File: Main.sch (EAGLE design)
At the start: 47 parts, among them IC1 LM75A, IC2 ADUM1400, IC3 74LS14N, Q1 IRF9530, U1 L298, U2 LM 1084 IT5,0, U3 LM 1084 IT3,3, U4 L298, X1 Motors, X2 PIRs, X3 Battery, X4 Ultra Sonics

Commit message: playing with routes
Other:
- moved on the sheet: F2, IC2, SV1

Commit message: cleanup and started to add servo control
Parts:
- added OK3: PC847, optocoupler:PC847
- added R10, R11, R12, R13: 120, resistor:R-EU_R0805
- added X5: ITG-3200, con-wago:233-504
- added X6: PIRs, con-wago:233-506
- X2: value PIRs -> (none); device con-wago:233-512 -> con-ria-59:AKL59-04
- X4: value Ultra Sonics -> Ultra Sonics (5V); device con-wago:233-508 -> con-wago:233-506
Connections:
- new net N$13: OK3A.A, R10.2
- new net N$21: OK3B.A, R11.2
- new net N$23: OK3C.A, R12.2
- new net N$25: OK3D.A, R13.2
- net +12V: now also X2-1.1
- net +3.3V: now also X2-3.1, X5.B-1
- net +5V: now also OK3A.COL, OK3B.COL, X2-2.1, X6.B-5; no longer X2.B-12, X2.B-3, X2.B-6, X2.B-9, X4.B-7
- net GND: now also OK3A.C, OK3B.C, OK3C.C, OK3D.C, X2-4.1, X5.B-2, X6.B-6; no longer X2.B-1, X2.B-10, X2.B-4, X2.B-7, X4.B-8
- net PIR1: now also X6.B-1; no longer X2.B-2
- net PIR2: now also X6.B-2; no longer X2.B-5
- net PIR3: now also X6.B-3; no longer X2.B-8
- net PIR4: now also X6.B-4; no longer X2.B-11
- net SCL1: now also X5.B-4
- net SDA1: now also X5.B-3

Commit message: optimizing board
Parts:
- X6: value PIRs -> PIRs (5V); device con-wago:233-506 -> con-wago:233-504
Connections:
- net +5V: no longer X6.B-5
- net GND: no longer X6.B-6
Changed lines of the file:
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@@
 <part name="OK3" library="optocoupler" deviceset="PC847" device=""/>
 <part name="X5" library="con-wago" deviceset="233-504" device="" value="ITG-3200"/>
-<part name="X6" library="con-wago" deviceset="233-506" device="" value="PIRs"/>
-<part name="GND17" library="supply1" deviceset="GND" device=""/>
+<part name="X6" library="con-wago" deviceset="233-504" device="" value="PIRs (5V)"/>
 <part name="R10" library="resistor" deviceset="R-EU_" device="R0805" value="120"/>
 <part name="R11" library="resistor" deviceset="R-EU_" device="R0805" value="120"/>
@@
 <instance part="OK3" gate="D" x="-386.08" y="-302.26"/>
 <instance part="X5" gate="G$1" x="-441.96" y="-533.4"/>
-<instance part="X6" gate="G$1" x="-429.26" y="-15.24"/>
-<instance part="GND17" gate="1" x="-454.66" y="-27.94"/>
+<instance part="X6" gate="G$1" x="-429.26" y="-12.7"/>
 <instance part="R10" gate="G$1" x="-406.4" y="-246.38"/>
 <instance part="R11" gate="G$1" x="-406.4" y="-264.16"/>
@@
 <junction x="-457.2" y="513.08"/>
 <label x="-474.98" y="513.08" size="1.778" layer="95"/>
-</segment>
-<segment>
-<pinref part="X6" gate="G$1" pin="B-5"/>
-<wire x1="-436.88" y1="-20.32" x2="-454.66" y2="-20.32" width="0.1524" layer="91"/>
-<label x="-454.66" y="-20.32" size="1.778" layer="95"/>
 </segment>
 <segment>
@@
 </segment>
 <segment>
-<pinref part="X6" gate="G$1" pin="B-6"/>
-<wire x1="-436.88" y1="-22.86" x2="-454.66" y2="-22.86" width="0.1524" layer="91"/>
-<label x="-454.66" y="-22.86" size="1.778" layer="95"/>
-<pinref part="GND17" gate="1" pin="GND"/>
-<wire x1="-454.66" y1="-22.86" x2="-454.66" y2="-25.4" width="0.1524" layer="91"/>
-</segment>
-<segment>

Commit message: optimizing board
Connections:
- net PIR1: now also SV1.32; no longer SV1.40
- net PIR4: now also SV1.40; no longer SV1.32
- net SCL1: now also X5.B-3; no longer X5.B-4
- net SDA1: now also X5.B-4; no longer X5.B-3
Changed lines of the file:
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@@
 <net name="PIR1" class="0">
-<segment>
-<pinref part="SV1" gate="G$1" pin="40"/>
-<wire x1="-345.44" y1="528.32" x2="-320.04" y2="528.32" width="0.1524" layer="91"/>
-<label x="-320.04" y="528.32" size="1.778" layer="95"/>
-</segment>
 <segment>
 <pinref part="X6" gate="G$1" pin="B-1"/>
 <wire x1="-436.88" y1="-10.16" x2="-454.66" y2="-10.16" width="0.1524" layer="91"/>
 <label x="-454.66" y="-10.16" size="1.778" layer="95"/>
+</segment>
+<segment>
+<pinref part="SV1" gate="G$1" pin="32"/>
+<wire x1="-345.44" y1="518.16" x2="-320.04" y2="518.16" width="0.1524" layer="91"/>
+<label x="-320.04" y="518.16" size="1.778" layer="95"/>
 </segment>
 </net>
@@
 <net name="PIR4" class="0">
 <segment>
-<pinref part="SV1" gate="G$1" pin="32"/>
-<wire x1="-345.44" y1="518.16" x2="-320.04" y2="518.16" width="0.1524" layer="91"/>
-<label x="-320.04" y="518.16" size="1.778" layer="95"/>
-</segment>
-<segment>
 <pinref part="X6" gate="G$1" pin="B-4"/>
 <wire x1="-436.88" y1="-17.78" x2="-454.66" y2="-17.78" width="0.1524" layer="91"/>
 <label x="-454.66" y="-17.78" size="1.778" layer="95"/>
+</segment>
+<segment>
+<pinref part="SV1" gate="G$1" pin="40"/>
+<wire x1="-345.44" y1="528.32" x2="-320.04" y2="528.32" width="0.1524" layer="91"/>
+<label x="-320.04" y="528.32" size="1.778" layer="95"/>
 </segment>
 </net>
@@
 </segment>
 <segment>
-<pinref part="X5" gate="G$1" pin="B-3"/>
-<wire x1="-449.58" y1="-535.94" x2="-487.68" y2="-535.94" width="0.1524" layer="91"/>
-<label x="-487.68" y="-535.94" size="1.778" layer="95"/>
+<pinref part="X5" gate="G$1" pin="B-4"/>
+<wire x1="-449.58" y1="-538.48" x2="-487.68" y2="-538.48" width="0.1524" layer="91"/>
+<label x="-487.68" y="-538.48" size="1.778" layer="95"/>
 </segment>
 </net>
@@
 </segment>
 <segment>
-<pinref part="X5" gate="G$1" pin="B-4"/>
-<wire x1="-449.58" y1="-538.48" x2="-487.68" y2="-538.48" width="0.1524" layer="91"/>
-<label x="-487.68" y="-538.48" size="1.778" layer="95"/>
+<pinref part="X5" gate="G$1" pin="B-3"/>
+<wire x1="-449.58" y1="-535.94" x2="-487.68" y2="-535.94" width="0.1524" layer="91"/>
+<label x="-487.68" y="-535.94" size="1.778" layer="95"/>
 </segment>
 </net>

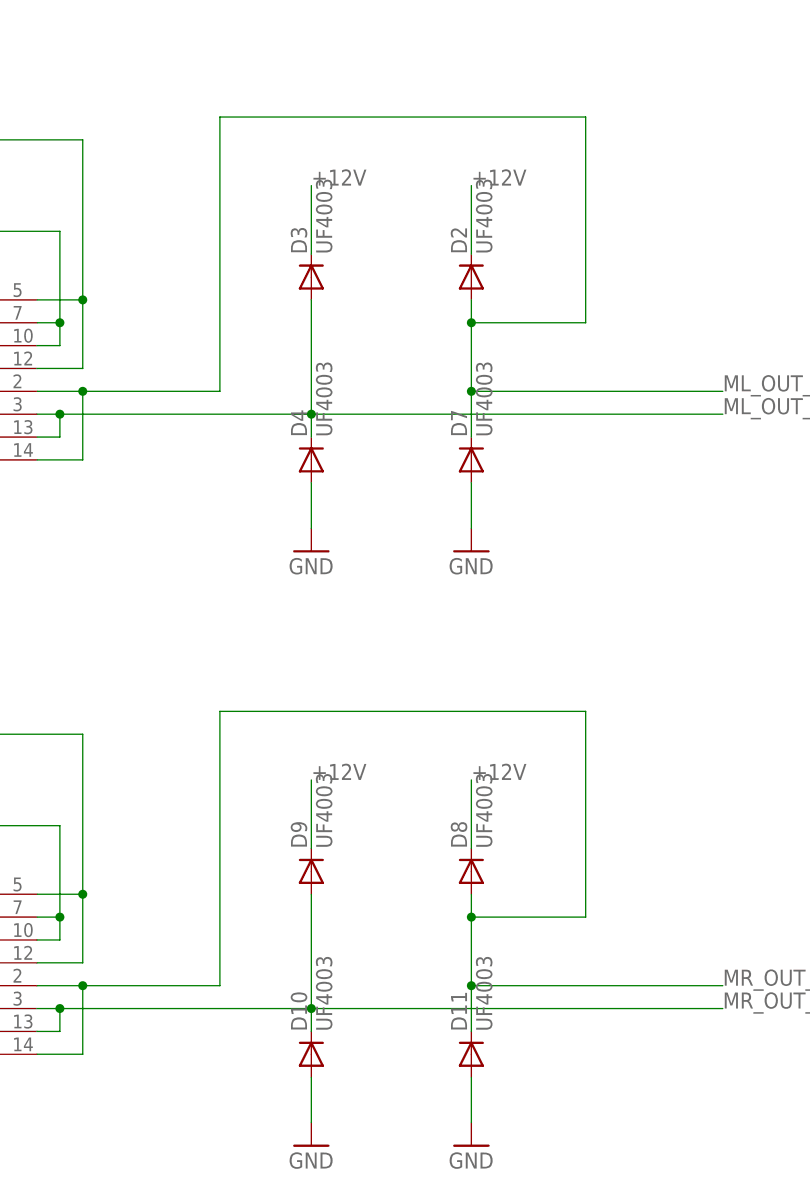
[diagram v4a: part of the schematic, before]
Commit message: smd protection diodes for h bridge
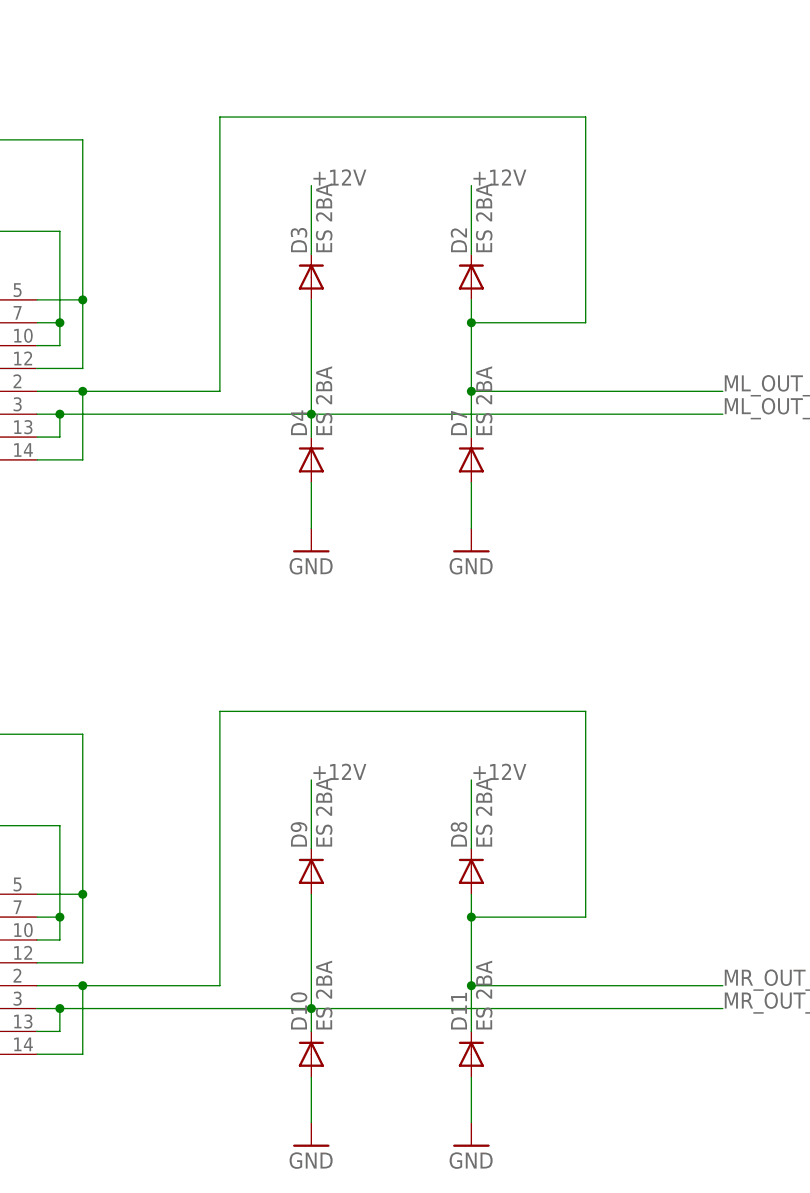
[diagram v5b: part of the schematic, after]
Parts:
- D10, D11, D2, D3, D4, D7, D8, D9: value UF4003 -> ES 2BA; device diode:UF4003 -> diode:ES2D
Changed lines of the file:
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@@
 <part name="SV1" library="con-lsta" deviceset="FE20-2" device="" value="Raspberry Pi B Plus Connector"/>
 <part name="GND4" library="supply1" deviceset="GND" device=""/>
-<part name="D2" library="diode" deviceset="UF4003" device="" value="UF4003"/>
-<part name="D3" library="diode" deviceset="UF4003" device="" value="UF4003"/>
-<part name="D4" library="diode" deviceset="UF4003" device="" value="UF4003"/>
-<part name="D7" library="diode" deviceset="UF4003" device="" value="UF4003"/>
+<part name="D2" library="diode" deviceset="ES2D" device="" value="ES 2BA"/>
+<part name="D3" library="diode" deviceset="ES2D" device="" value="ES 2BA"/>
+<part name="D4" library="diode" deviceset="ES2D" device="" value="ES 2BA"/>
+<part name="D7" library="diode" deviceset="ES2D" device="" value="ES 2BA"/>
 <part name="GND2" library="supply1" deviceset="GND" device=""/>
 <part name="GND5" library="supply1" deviceset="GND" device=""/>
@@
 <part name="C8" library="rcl" deviceset="C-EU" device="C0805" value="100nF"/>
 <part name="GND6" library="supply1" deviceset="GND" device=""/>
-<part name="D8" library="diode" deviceset="UF4003" device="" value="UF4003"/>
-<part name="D9" library="diode" deviceset="UF4003" device="" value="UF4003"/>
-<part name="D10" library="diode" deviceset="UF4003" device="" value="UF4003"/>
-<part name="D11" library="diode" deviceset="UF4003" device="" value="UF4003"/>
+<part name="D8" library="diode" deviceset="ES2D" device="" value="ES 2BA"/>
+<part name="D9" library="diode" deviceset="ES2D" device="" value="ES 2BA"/>
+<part name="D10" library="diode" deviceset="ES2D" device="" value="ES 2BA"/>
+<part name="D11" library="diode" deviceset="ES2D" device="" value="ES 2BA"/>
 <part name="GND7" library="supply1" deviceset="GND" device=""/>
 <part name="GND8" library="supply1" deviceset="GND" device=""/>
@@
 <instance part="SV1" gate="G$1" x="-353.06" y="505.46"/>
 <instance part="GND4" gate="1" x="-304.8" y="482.6"/>
-<instance part="D2" gate="1" x="-309.88" y="172.72" rot="R90"/>
-<instance part="D3" gate="1" x="-327.66" y="172.72" rot="R90"/>
-<instance part="D4" gate="1" x="-327.66" y="152.4" rot="R90"/>
-<instance part="D7" gate="1" x="-309.88" y="152.4" rot="R90"/>
+<instance part="D2" gate="G$1" x="-309.88" y="172.72" rot="R90"/>
+<instance part="D3" gate="G$1" x="-327.66" y="172.72" rot="R90"/>
+<instance part="D4" gate="G$1" x="-327.66" y="152.4" rot="R90"/>
+<instance part="D7" gate="G$1" x="-309.88" y="152.4" rot="R90"/>
 <instance part="GND2" gate="1" x="-327.66" y="142.24"/>
 <instance part="GND5" gate="1" x="-309.88" y="142.24"/>
@@
 <instance part="C8" gate="G$1" x="-398.78" y="88.9"/>
 <instance part="GND6" gate="1" x="-416.56" y="76.2"/>
-<instance part="D8" gate="1" x="-309.88" y="106.68" rot="R90"/>
-<instance part="D9" gate="1" x="-327.66" y="106.68" rot="R90"/>
-<instance part="D10" gate="1" x="-327.66" y="86.36" rot="R90"/>
-<instance part="D11" gate="1" x="-309.88" y="86.36" rot="R90"/>
+<instance part="D8" gate="G$1" x="-309.88" y="106.68" rot="R90"/>
+<instance part="D9" gate="G$1" x="-327.66" y="106.68" rot="R90"/>
+<instance part="D10" gate="G$1" x="-327.66" y="86.36" rot="R90"/>
+<instance part="D11" gate="G$1" x="-309.88" y="86.36" rot="R90"/>
 <instance part="GND7" gate="1" x="-327.66" y="76.2"/>
 <instance part="GND8" gate="1" x="-309.88" y="76.2"/>
@@
 </segment>
 <segment>
-<pinref part="D3" gate="1" pin="C"/>
+<pinref part="D3" gate="G$1" pin="C"/>
 <wire x1="-327.66" y1="175.26" x2="-327.66" y2="182.88" width="0.1524" layer="91"/>
 <label x="-327.66" y="182.88" size="1.778" layer="95"/>
 </segment>
 <segment>
-<pinref part="D2" gate="1" pin="C"/>
+<pinref part="D2" gate="G$1" pin="C"/>
 <wire x1="-309.88" y1="175.26" x2="-309.88" y2="182.88" width="0.1524" layer="91"/>
 <label x="-309.88" y="182.88" size="1.778" layer="95"/>
@@
 </segment>
 <segment>
-<pinref part="D9" gate="1" pin="C"/>
+<pinref part="D9" gate="G$1" pin="C"/>
 <wire x1="-327.66" y1="109.22" x2="-327.66" y2="116.84" width="0.1524" layer="91"/>
 <label x="-327.66" y="116.84" size="1.778" layer="95"/>
 </segment>
 <segment>
-<pinref part="D8" gate="1" pin="C"/>
+<pinref part="D8" gate="G$1" pin="C"/>
 <wire x1="-309.88" y1="109.22" x2="-309.88" y2="116.84" width="0.1524" layer="91"/>
 <label x="-309.88" y="116.84" size="1.778" layer="95"/>
@@
 <segment>
 <pinref part="GND2" gate="1" pin="GND"/>
-<pinref part="D4" gate="1" pin="A"/>
+<pinref part="D4" gate="G$1" pin="A"/>
 <wire x1="-327.66" y1="144.78" x2="-327.66" y2="149.86" width="0.1524" layer="91"/>
 </segment>
 <segment>
 <pinref part="GND5" gate="1" pin="GND"/>
-<pinref part="D7" gate="1" pin="A"/>
+<pinref part="D7" gate="G$1" pin="A"/>
 <wire x1="-309.88" y1="144.78" x2="-309.88" y2="149.86" width="0.1524" layer="91"/>
 </segment>
@@
 <segment>
 <pinref part="GND7" gate="1" pin="GND"/>
-<pinref part="D10" gate="1" pin="A"/>
+<pinref part="D10" gate="G$1" pin="A"/>
 <wire x1="-327.66" y1="78.74" x2="-327.66" y2="83.82" width="0.1524" layer="91"/>
 </segment>
 <segment>
 <pinref part="GND8" gate="1" pin="GND"/>
-<pinref part="D11" gate="1" pin="A"/>
+<pinref part="D11" gate="G$1" pin="A"/>
 <wire x1="-309.88" y1="78.74" x2="-309.88" y2="83.82" width="0.1524" layer="91"/>
 </segment>
@@
 <net name="ML_OUT_B" class="2">
 <segment>
-<pinref part="D3" gate="1" pin="A"/>
-<pinref part="D4" gate="1" pin="C"/>
+<pinref part="D3" gate="G$1" pin="A"/>
+<pinref part="D4" gate="G$1" pin="C"/>
 <wire x1="-327.66" y1="170.18" x2="-327.66" y2="157.48" width="0.1524" layer="91"/>
 <pinref part="U1" gate="G$1" pin="OUT2"/>
@@
 <net name="ML_OUT_A" class="2">
 <segment>
-<pinref part="D2" gate="1" pin="A"/>
-<pinref part="D7" gate="1" pin="C"/>
+<pinref part="D2" gate="G$1" pin="A"/>
+<pinref part="D7" gate="G$1" pin="C"/>
 <wire x1="-309.88" y1="170.18" x2="-309.88" y2="167.64" width="0.1524" layer="91"/>
 <pinref part="U1" gate="G$1" pin="OUT1"/>
@@
 <net name="MR_OUT_A" class="2">
 <segment>
-<pinref part="D8" gate="1" pin="A"/>
-<pinref part="D11" gate="1" pin="C"/>
+<pinref part="D8" gate="G$1" pin="A"/>
+<pinref part="D11" gate="G$1" pin="C"/>
 <wire x1="-309.88" y1="104.14" x2="-309.88" y2="101.6" width="0.1524" layer="91"/>
 <pinref part="U4" gate="G$1" pin="OUT1"/>
@@
 <net name="MR_OUT_B" class="2">
 <segment>
-<pinref part="D9" gate="1" pin="A"/>
-<pinref part="D10" gate="1" pin="C"/>
+<pinref part="D9" gate="G$1" pin="A"/>
+<pinref part="D10" gate="G$1" pin="C"/>
 <wire x1="-327.66" y1="104.14" x2="-327.66" y2="91.44" width="0.1524" layer="91"/>
 <pinref part="U4" gate="G$1" pin="OUT2"/>

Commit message: gpio expander
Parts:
- added IC4: MCP2300X/P, adafruit:MCP2300X/P
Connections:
- net N$1 renamed ML_DIR_
- net N$12 renamed MR_SPEED_
- net N$6 renamed ML_SPEED_
- net N$8 renamed MR_DIR_
- new net CAM_SERVO_AZI: OK3A.EMIT
- new net CAM_SERVO_ELE: OK3B.EMIT
- new net N$1: IC4.GP0
- new net N$12: IC4.GP3
- new net N$27: IC4.GP4
- new net N$28: IC4.GP5
- new net N$29: IC4.GP6
- new net N$31: IC4.GP7
- new net N$35: IC4./RST
- new net N$37: IC4.INT
- new net N$40: IC4.A0
- new net N$41: IC4.A1
- new net N$42: IC4.A2
- new net N$6: IC4.GP1
- new net N$8: IC4.GP2
- net SCL1: now also IC4.SCL
- net SDA1: now also IC4.SDA
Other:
- moved on the sheet: F2, IC2, OK3A, OK3B, OK3C, OK3D, R10, R11, R12, R13, SV1
